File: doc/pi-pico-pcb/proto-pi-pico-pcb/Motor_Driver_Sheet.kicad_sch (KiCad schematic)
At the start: 5 parts

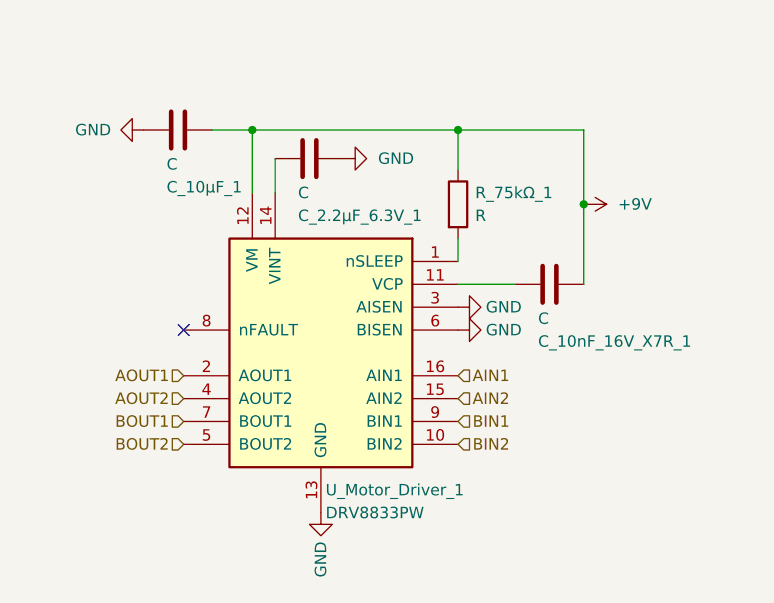
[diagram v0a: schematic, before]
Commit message: converted ports to nested sheets
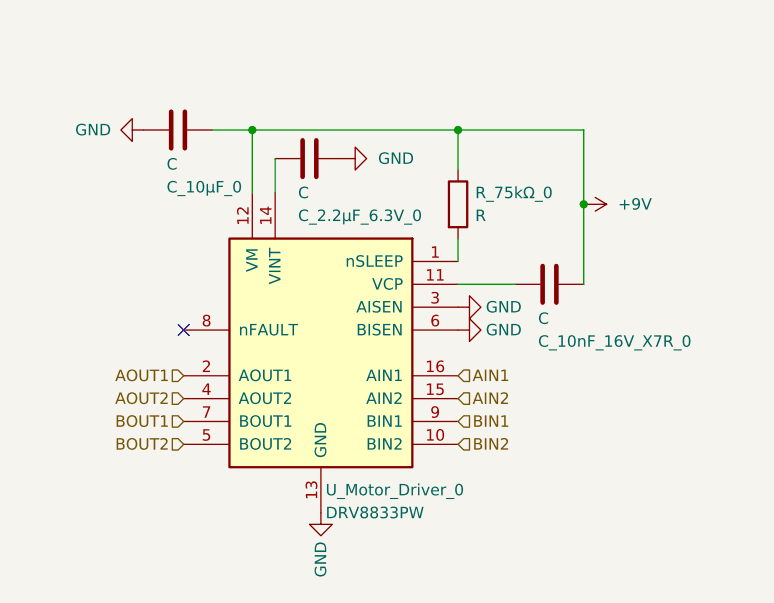
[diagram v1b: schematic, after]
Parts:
- renumbered C_10nF_16V_X7R_1 to C_10nF_16V_X7R_0, C_10μF_1 to C_10μF_0, C_2.2μF_6.3V_1 to C_2.2μF_6.3V_0, R_75kΩ_1 to R_75kΩ_0, U_Motor_Driver_1 to U_Motor_Driver_0
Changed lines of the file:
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@@
   (symbol (lib_id "Device:C") (at 140.335 87.63 270) (unit 1)
     (in_bom yes) (on_board yes)
-    (property "Reference" "C_2.2μF_6.3V_1" (id 0) (at 139.065 93.98 90)
+    (property "Reference" "C_2.2μF_6.3V_0" (id 0) (at 139.065 93.98 90)
       (effects (font (size 1.27 1.27)) (justify left))
     )
@@
   (symbol (lib_id "Device:C") (at 167.005 101.6 270) (unit 1)
     (in_bom yes) (on_board yes)
-    (property "Reference" "C_10nF_16V_X7R_1" (id 0) (at 165.735 107.95 90)
+    (property "Reference" "C_10nF_16V_X7R_0" (id 0) (at 165.735 107.95 90)
       (effects (font (size 1.27 1.27)) (justify left))
     )
@@
   (symbol (lib_id "power:GND") (at 156.845 104.14 90) (unit 1)
     (in_bom yes) (on_board yes)
-    (property "Reference" "#PWR0110" (id 0) (at 163.195 104.14 0)
+    (property "Reference" "#PWR0134" (id 0) (at 163.195 104.14 0)
       (effects (font (size 1.27 1.27)) hide)
     )
@@
   (symbol (lib_id "power:GND") (at 121.92 84.455 270) (unit 1)
     (in_bom yes) (on_board yes)
-    (property "Reference" "#PWR0102" (id 0) (at 115.57 84.455 0)
+    (property "Reference" "#PWR0132" (id 0) (at 115.57 84.455 0)
       (effects (font (size 1.27 1.27)) hide)
     )
@@
   (symbol (lib_id "power:GND") (at 144.145 87.63 90) (mirror x) (unit 1)
     (in_bom yes) (on_board yes)
-    (property "Reference" "#PWR0101" (id 0) (at 150.495 87.63 0)
+    (property "Reference" "#PWR0128" (id 0) (at 150.495 87.63 0)
       (effects (font (size 1.27 1.27)) hide)
     )
@@
   (symbol (lib_id "Driver_Motor:DRV8833PW") (at 141.605 109.22 0) (mirror y) (unit 1)
     (in_bom yes) (on_board yes) (fields_autoplaced)
-    (property "Reference" "U_Motor_Driver_1" (id 0) (at 142.1256 124.46 0)
+    (property "Reference" "U_Motor_Driver_0" (id 0) (at 142.1256 124.46 0)
       (effects (font (size 1.27 1.27)) (justify right))
     )
@@
   (symbol (lib_id "Device:R") (at 156.845 92.71 0) (unit 1)
     (in_bom yes) (on_board yes) (fields_autoplaced)
-    (property "Reference" "R_75kΩ_1" (id 0) (at 158.75 91.4399 0)
+    (property "Reference" "R_75kΩ_0" (id 0) (at 158.75 91.4399 0)
       (effects (font (size 1.27 1.27)) (justify left))
     )
@@
   (symbol (lib_id "Device:C") (at 125.73 84.455 270) (unit 1)
     (in_bom yes) (on_board yes)
-    (property "Reference" "C_10μF_1" (id 0) (at 124.46 90.805 90)
+    (property "Reference" "C_10μF_0" (id 0) (at 124.46 90.805 90)
       (effects (font (size 1.27 1.27)) (justify left))
     )
@@
   (symbol (lib_id "power:GND") (at 141.605 127 0) (mirror y) (unit 1)
     (in_bom yes) (on_board yes)
-    (property "Reference" "#PWR0113" (id 0) (at 141.605 133.35 0)
+    (property "Reference" "#PWR0136" (id 0) (at 141.605 133.35 0)
       (effects (font (size 1.27 1.27)) hide)
     )
@@
   (symbol (lib_id "power:+9V") (at 170.815 92.71 270) (mirror x) (unit 1)
     (in_bom yes) (on_board yes) (fields_autoplaced)
-    (property "Reference" "#PWR0109" (id 0) (at 167.005 92.71 0)
+    (property "Reference" "#PWR0133" (id 0) (at 167.005 92.71 0)
       (effects (font (size 1.27 1.27)) hide)
     )
@@
   (symbol (lib_id "power:GND") (at 156.845 106.68 90) (unit 1)
     (in_bom yes) (on_board yes)
-    (property "Reference" "#PWR0112" (id 0) (at 163.195 106.68 0)
+    (property "Reference" "#PWR0135" (id 0) (at 163.195 106.68 0)
       (effects (font (size 1.27 1.27)) hide)
     )

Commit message: added flash memory
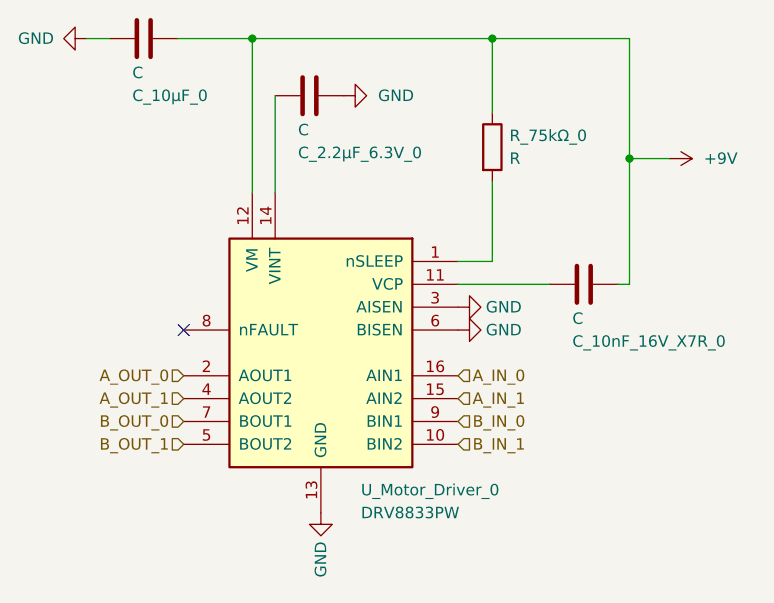
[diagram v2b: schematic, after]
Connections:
- net AIN1 renamed A_IN_0
- net AIN2 renamed A_IN_1
- net AOUT1 renamed A_OUT_0
- net AOUT2 renamed A_OUT_1
- net BIN1 renamed B_IN_0
- net BIN2 renamed B_IN_1
- net BOUT1 renamed B_OUT_0
- net BOUT2 renamed B_OUT_1
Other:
- company: (none) -> PROTO
- moved on the sheet: C_10nF_16V_X7R_0, C_10μF_0, C_2.2μF_6.3V_0, R_75kΩ_0
